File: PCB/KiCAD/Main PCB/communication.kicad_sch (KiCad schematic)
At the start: 2 parts, among them IC3 XB3-24Z8CM, J4 Conn_Coaxial_Small

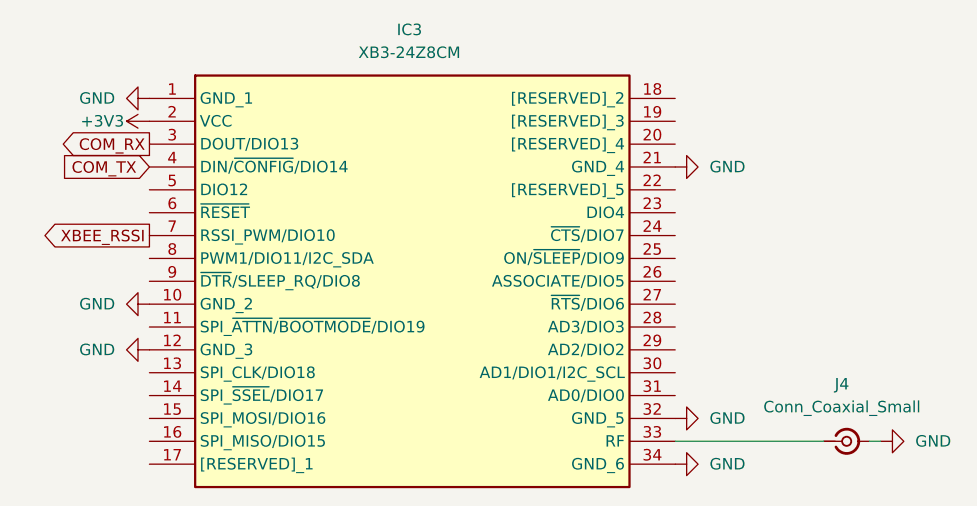
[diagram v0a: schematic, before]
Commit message: New motor controllers for the main PCB
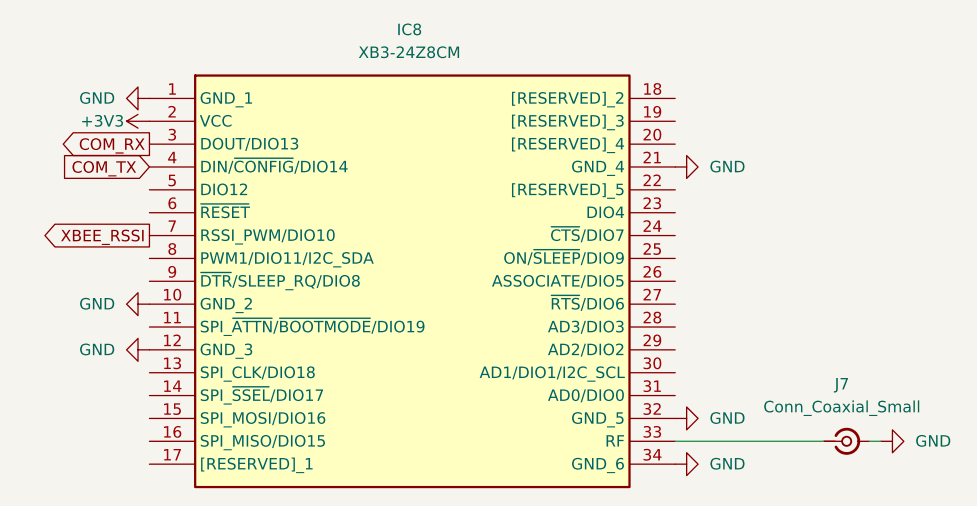
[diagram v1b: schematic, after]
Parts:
- renumbered IC3 to IC8, J4 to J7
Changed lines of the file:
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@@
 		(dnp no)
 		(fields_autoplaced yes)
-		(property "Reference" "#PWR0105"
+		(property "Reference" "#PWR0123"
 			(at 181.61 109.22 0)
 			(effects
@@
 			(project "Main PCB"
 				(path "/2fa7e914-8c49-49b7-a5a9-3cb78b2e953f/ab22dc4d-1004-4b41-8ca9-5648e42ab9ec"
-					(reference "#PWR0105")
+					(reference "#PWR0123")
 					(unit 1)
 				)
@@
 		(dnp no)
 		(fields_autoplaced yes)
-		(property "Reference" "J4"
+		(property "Reference" "J7"
 			(at 193.7904 100.33 0)
 			(effects
@@
 			(project ""
 				(path "/2fa7e914-8c49-49b7-a5a9-3cb78b2e953f/ab22dc4d-1004-4b41-8ca9-5648e42ab9ec"
-					(reference "J4")
+					(reference "J7")
 					(unit 1)
 				)
@@
 		(dnp no)
 		(fields_autoplaced yes)
-		(property "Reference" "#PWR0103"
+		(property "Reference" "#PWR0121"
 			(at 181.61 76.2 0)
 			(effects
@@
 			(project "Main PCB"
 				(path "/2fa7e914-8c49-49b7-a5a9-3cb78b2e953f/ab22dc4d-1004-4b41-8ca9-5648e42ab9ec"
-					(reference "#PWR0103")
+					(reference "#PWR0121")
 					(unit 1)
 				)
@@
 		(dnp no)
 		(fields_autoplaced yes)
-		(property "Reference" "#PWR096"
+		(property "Reference" "#PWR0120"
 			(at 110.49 96.52 0)
 			(effects
@@
 			(project "Main PCB"
 				(path "/2fa7e914-8c49-49b7-a5a9-3cb78b2e953f/ab22dc4d-1004-4b41-8ca9-5648e42ab9ec"
-					(reference "#PWR096")
+					(reference "#PWR0120")
 					(unit 1)
 				)
@@
 		(dnp no)
 		(fields_autoplaced yes)
-		(property "Reference" "#PWR093"
+		(property "Reference" "#PWR0117"
 			(at 110.49 68.58 0)
 			(effects
@@
 			(project "Main PCB"
 				(path "/2fa7e914-8c49-49b7-a5a9-3cb78b2e953f/ab22dc4d-1004-4b41-8ca9-5648e42ab9ec"
-					(reference "#PWR093")
+					(reference "#PWR0117")
 					(unit 1)
 				)
@@
 		(dnp no)
 		(fields_autoplaced yes)
-		(property "Reference" "#PWR0106"
+		(property "Reference" "#PWR0124"
 			(at 204.47 106.68 0)
 			(effects
@@
 			(project "Main PCB"
 				(path "/2fa7e914-8c49-49b7-a5a9-3cb78b2e953f/ab22dc4d-1004-4b41-8ca9-5648e42ab9ec"
-					(reference "#PWR0106")
+					(reference "#PWR0124")
 					(unit 1)
 				)
@@
 		(on_board yes)
 		(dnp no)
-		(property "Reference" "#PWR094"
+		(property "Reference" "#PWR0118"
 			(at 120.65 71.12 0)
 			(effects
@@
 			(project "Main PCB"
 				(path "/2fa7e914-8c49-49b7-a5a9-3cb78b2e953f/ab22dc4d-1004-4b41-8ca9-5648e42ab9ec"
-					(reference "#PWR094")
+					(reference "#PWR0118")
 					(unit 1)
 				)
@@
 		(dnp no)
 		(fields_autoplaced yes)
-		(property "Reference" "#PWR095"
+		(property "Reference" "#PWR0119"
 			(at 110.49 91.44 0)
 			(effects
@@
 			(project "Main PCB"
 				(path "/2fa7e914-8c49-49b7-a5a9-3cb78b2e953f/ab22dc4d-1004-4b41-8ca9-5648e42ab9ec"
-					(reference "#PWR095")
+					(reference "#PWR0119")
 					(unit 1)
 				)
@@
 		(dnp no)
 		(fields_autoplaced yes)
-		(property "Reference" "#PWR0104"
+		(property "Reference" "#PWR0122"
 			(at 181.61 104.14 0)
 			(effects
@@
 			(project "Main PCB"
 				(path "/2fa7e914-8c49-49b7-a5a9-3cb78b2e953f/ab22dc4d-1004-4b41-8ca9-5648e42ab9ec"
-					(reference "#PWR0104")
+					(reference "#PWR0122")
 					(unit 1)
 				)
@@
 		(dnp no)
 		(fields_autoplaced yes)
-		(property "Reference" "IC3"
+		(property "Reference" "IC8"
 			(at 145.7325 60.96 0)
 			(effects
@@
 			(project ""
 				(path "/2fa7e914-8c49-49b7-a5a9-3cb78b2e953f/ab22dc4d-1004-4b41-8ca9-5648e42ab9ec"
-					(reference "IC3")
-					(unit 1)
-				)
+					(reference "IC8")
+					(unit 1)
+				)

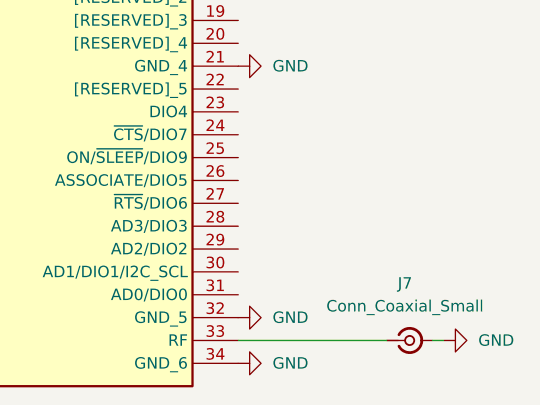
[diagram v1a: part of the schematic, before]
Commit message: Added a BNO055 and traced PCB (incomplete, no DRC pass)
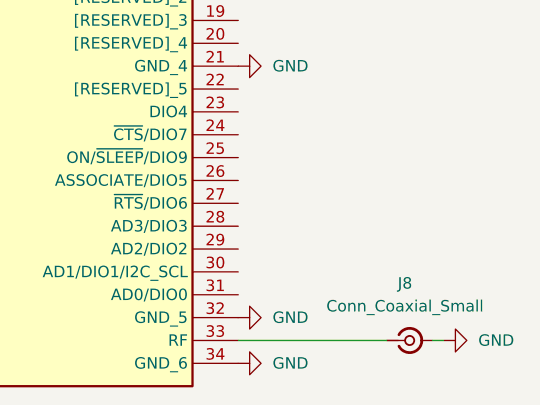
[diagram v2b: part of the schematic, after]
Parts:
- renumbered J7 to J8
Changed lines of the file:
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@@
 		(dnp no)
 		(fields_autoplaced yes)
-		(property "Reference" "#PWR0123"
+		(property "Reference" "#PWR0127"
 			(at 181.61 109.22 0)
 			(effects
@@
 			(project "Main PCB"
 				(path "/2fa7e914-8c49-49b7-a5a9-3cb78b2e953f/ab22dc4d-1004-4b41-8ca9-5648e42ab9ec"
-					(reference "#PWR0123")
+					(reference "#PWR0127")
 					(unit 1)
 				)
@@
 		(dnp no)
 		(fields_autoplaced yes)
-		(property "Reference" "J7"
+		(property "Reference" "J8"
 			(at 193.7904 100.33 0)
 			(effects
@@
 			(project ""
 				(path "/2fa7e914-8c49-49b7-a5a9-3cb78b2e953f/ab22dc4d-1004-4b41-8ca9-5648e42ab9ec"
-					(reference "J7")
+					(reference "J8")
 					(unit 1)
 				)
@@
 		(dnp no)
 		(fields_autoplaced yes)
-		(property "Reference" "#PWR0121"
+		(property "Reference" "#PWR0125"
 			(at 181.61 76.2 0)
 			(effects
@@
 			(project "Main PCB"
 				(path "/2fa7e914-8c49-49b7-a5a9-3cb78b2e953f/ab22dc4d-1004-4b41-8ca9-5648e42ab9ec"
-					(reference "#PWR0121")
+					(reference "#PWR0125")
 					(unit 1)
 				)
@@
 		(dnp no)
 		(fields_autoplaced yes)
-		(property "Reference" "#PWR0120"
+		(property "Reference" "#PWR0124"
 			(at 110.49 96.52 0)
 			(effects
@@
 			(project "Main PCB"
 				(path "/2fa7e914-8c49-49b7-a5a9-3cb78b2e953f/ab22dc4d-1004-4b41-8ca9-5648e42ab9ec"
-					(reference "#PWR0120")
+					(reference "#PWR0124")
 					(unit 1)
 				)
@@
 		(dnp no)
 		(fields_autoplaced yes)
-		(property "Reference" "#PWR0117"
+		(property "Reference" "#PWR0121"
 			(at 110.49 68.58 0)
 			(effects
@@
 			(project "Main PCB"
 				(path "/2fa7e914-8c49-49b7-a5a9-3cb78b2e953f/ab22dc4d-1004-4b41-8ca9-5648e42ab9ec"
-					(reference "#PWR0117")
+					(reference "#PWR0121")
 					(unit 1)
 				)
@@
 		(dnp no)
 		(fields_autoplaced yes)
-		(property "Reference" "#PWR0124"
+		(property "Reference" "#PWR0128"
 			(at 204.47 106.68 0)
 			(effects
@@
 			(project "Main PCB"
 				(path "/2fa7e914-8c49-49b7-a5a9-3cb78b2e953f/ab22dc4d-1004-4b41-8ca9-5648e42ab9ec"
-					(reference "#PWR0124")
+					(reference "#PWR0128")
 					(unit 1)
 				)
@@
 		(on_board yes)
 		(dnp no)
-		(property "Reference" "#PWR0118"
+		(property "Reference" "#PWR0122"
 			(at 120.65 71.12 0)
 			(effects
@@
 			(project "Main PCB"
 				(path "/2fa7e914-8c49-49b7-a5a9-3cb78b2e953f/ab22dc4d-1004-4b41-8ca9-5648e42ab9ec"
-					(reference "#PWR0118")
+					(reference "#PWR0122")
 					(unit 1)
 				)
@@
 		(dnp no)
 		(fields_autoplaced yes)
-		(property "Reference" "#PWR0119"
+		(property "Reference" "#PWR0123"
 			(at 110.49 91.44 0)
 			(effects
@@
 			(project "Main PCB"
 				(path "/2fa7e914-8c49-49b7-a5a9-3cb78b2e953f/ab22dc4d-1004-4b41-8ca9-5648e42ab9ec"
-					(reference "#PWR0119")
+					(reference "#PWR0123")
 					(unit 1)
 				)
@@
 		(dnp no)
 		(fields_autoplaced yes)
-		(property "Reference" "#PWR0122"
+		(property "Reference" "#PWR0126"
 			(at 181.61 104.14 0)
 			(effects
@@
 			(project "Main PCB"
 				(path "/2fa7e914-8c49-49b7-a5a9-3cb78b2e953f/ab22dc4d-1004-4b41-8ca9-5648e42ab9ec"
-					(reference "#PWR0122")
-					(unit 1)
-				)
+					(reference "#PWR0126")
+					(unit 1)
+				)
